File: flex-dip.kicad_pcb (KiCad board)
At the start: 2 copper layers, 19.9 x 12.9 mm, 17 parts, among them J1 Conn_01x01_Female, J10 Conn_01x01_Female, J11 Conn_01x01_Female, J12 Conn_01x01_Female, J13 Conn_01x01_Female, J14 Conn_01x01_Female, J15 Conn_01x01_Female, J16 Conn_01x01_Female, J2 Conn_01x01_Female, J3 Conn_01x01_Female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

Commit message: add gerbers
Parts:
- added REF**: OSHW-Logo2_7.3x6mm_Copper, Symbol:OSHW-Logo2_7.3x6mm_Copper, B.Cu at (119.0, 67.9)
- added REF**: OSHW-Logo2_7.3x6mm_Copper, Symbol:OSHW-Logo2_7.3x6mm_Copper, F.Cu at (119.0, 67.9)
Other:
- board text added: "2020-03-03"
- board text added: "@HelenLeigh"
- board text removed: "2020-02-06"

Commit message: update silkscreen
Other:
- board text added: "Stitch and Glitch"
- board text removed: "Crackle Flex Sew Box"
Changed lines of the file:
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@@
       (effects (font (size 1 1) (thickness 0.15)))
     )
-    (fp_line (start -1.05 8.89) (end 8.67 8.89) (layer "F.CrtYd") (width 0.1))
-    (fp_line (start -1.05 -1.29) (end -1.05 8.89) (layer "F.CrtYd") (width 0.1))
-    (fp_line (start 8.67 -1.29) (end 8.67 8.89) (layer "F.CrtYd") (width 0.1))
-    (fp_line (start -1.05 -1.29) (end 8.67 -1.29) (layer "F.CrtYd") (width 0.1))
-    (fp_line (start 0.4 -0.9) (end 0.4 -1.2) (layer "F.SilkS") (width 0.1))
-    (fp_line (start 0.4 -1.2) (end 0.7 -1.2) (layer "F.SilkS") (width 0.1))
-    (fp_line (start 7.2 -0.9) (end 7.2 -1.2) (layer "F.SilkS") (width 0.1))
-    (fp_line (start 7.2 -1.2) (end 6.9 -1.2) (layer "F.SilkS") (width 0.1))
-    (fp_line (start 7.2 8.5) (end 7.2 8.8) (layer "F.SilkS") (width 0.1))
-    (fp_line (start 7.2 8.8) (end 6.9 8.8) (layer "F.SilkS") (width 0.1))
-    (fp_line (start 0.4 8.5) (end 0.4 8.8) (layer "F.SilkS") (width 0.1))
-    (fp_line (start 0.4 8.8) (end 0.7 8.8) (layer "F.SilkS") (width 0.1))
-    (fp_line (start 0.55 8.64) (end 7.05 8.64) (layer "F.Fab") (width 0.1))
-    (fp_line (start 0.55 -1.04) (end 7.05 -1.04) (layer "F.Fab") (width 0.1))
-    (fp_line (start 7.05 -1.04) (end 7.05 8.64) (layer "F.Fab") (width 0.1))
-    (fp_line (start 0.55 -1.04) (end 0.55 8.64) (layer "F.Fab") (width 0.1))
     (fp_text user "REF**" (at 3.94 3.49) (layer "F.Fab") hide
       (effects (font (size 1 1) (thickness 0.1)))
     )
+    (fp_line (start 0.55 -1.04) (end 0.55 8.64) (layer "F.Fab") (width 0.1))
+    (fp_line (start 7.05 -1.04) (end 7.05 8.64) (layer "F.Fab") (width 0.1))
+    (fp_line (start 0.55 -1.04) (end 7.05 -1.04) (layer "F.Fab") (width 0.1))
+    (fp_line (start 0.55 8.64) (end 7.05 8.64) (layer "F.Fab") (width 0.1))
+    (fp_line (start 0.4 8.8) (end 0.7 8.8) (layer "F.SilkS") (width 0.1))
+    (fp_line (start 0.4 8.5) (end 0.4 8.8) (layer "F.SilkS") (width 0.1))
+    (fp_line (start 7.2 8.8) (end 6.9 8.8) (layer "F.SilkS") (width 0.1))
+    (fp_line (start 7.2 8.5) (end 7.2 8.8) (layer "F.SilkS") (width 0.1))
+    (fp_line (start 7.2 -1.2) (end 6.9 -1.2) (layer "F.SilkS") (width 0.1))
+    (fp_line (start 7.2 -0.9) (end 7.2 -1.2) (layer "F.SilkS") (width 0.1))
+    (fp_line (start 0.4 -1.2) (end 0.7 -1.2) (layer "F.SilkS") (width 0.1))
+    (fp_line (start 0.4 -0.9) (end 0.4 -1.2) (layer "F.SilkS") (width 0.1))
+    (fp_line (start -1.05 -1.29) (end 8.67 -1.29) (layer "F.CrtYd") (width 0.1))
+    (fp_line (start 8.67 -1.29) (end 8.67 8.89) (layer "F.CrtYd") (width 0.1))
+    (fp_line (start -1.05 -1.29) (end -1.05 8.89) (layer "F.CrtYd") (width 0.1))
+    (fp_line (start -1.05 8.89) (end 8.67 8.89) (layer "F.CrtYd") (width 0.1))
     (pad "8" thru_hole circle (at 7.62 0) (size 1.6 1.6) (drill 1) (layers *.Cu *.Mask)
       (net 6 "Net-(J11-Pad1)"))
@@
     )
   )
-  (gr_text "Crackle Flex Sew Box" (at 119.26824 61.61532) (layer "B.SilkS")
+  (gr_text "Stitch and Glitch" (at 119.26824 61.61532) (layer "B.SilkS")
     (effects (font (size 0.9 1.016) (thickness 0.1016)) (justify mirror))
   )
@@
     (effects (font (size 1.016 1.016) (thickness 0.1016)) (justify mirror))
   )
-  (gr_text "Crackle Flex Sew Box" (at 119.28348 61.62802) (layer "F.SilkS")
+  (gr_text "Stitch and Glitch" (at 119.28348 61.62802) (layer "F.SilkS")
     (effects (font (size 0.9 1.016) (thickness 0.1016)))
   )
@@
   (gr_line (start 126.1872 80.18272) (end 126.1872 61.4426) (layer "Eco1.User") (width 0.1))
   (gr_line (start 111.83366 80.25638) (end 111.83366 61.51626) (layer "Eco1.User") (width 0.1))
+  (segment (start 126.20752 71.15556) (end 128.8669 71.16318) (width 0.25) (layer "F.Cu") (net 3))
+  (segment (start 122.776161 71.141741) (end 126.20752 71.15556) (width 0.25) (layer "F.Cu") (net 3))
+  (segment (start 126.15926 68.60794) (end 128.85928 68.6054) (width 0.25) (layer "F.Cu") (net 2))
+  (segment (start 122.776161 68.601741) (end 126.15926 68.60794) (width 0.25) (layer "F.Cu") (net 2))
+  (segment (start 126.20498 66.07048) (end 128.86944 66.07556) (width 0.25) (layer "F.Cu") (net 1))
+  (segment (start 122.776161 66.061741) (end 126.20498 66.07048) (width 0.25) (layer "F.Cu") (net 1))
+  (segment (start 126.18466 63.53302) (end 128.85674 63.53556) (width 0.25) (layer "F.Cu") (net 6))
+  (segment (start 122.776161 63.521741) (end 126.18466 63.53302) (width 0.25) (layer "F.Cu") (net 6))
+  (segment (start 111.83366 71.13524) (end 115.156161 71.141741) (width 0.25) (layer "F.Cu") (net 5))
+  (segment (start 108.96854 71.13778) (end 111.83366 71.13524) (width 0.25) (layer "F.Cu") (net 5))
+  (segment (start 111.8235 68.59778) (end 115.156161 68.601741) (width 0.25) (layer "F.Cu") (net 2))
+  (segment (start 108.97108 68.59016) (end 111.8235 68.59778) (width 0.25) (layer "F.Cu") (net 2))
+  (segment (start 108.96092 66.0654) (end 111.82858 66.0654) (width 0.25) (layer "F.Cu") (net 5))
+  (segment (start 111.82858 66.0654) (end 115.156161 66.061741) (width 0.3) (layer "F.Cu") (net 5))
+  (segment (start 111.82858 63.52286) (end 115.156161 63.521741) (width 0.3) (layer "F.Cu") (net 4))
   (segment (start 108.95584 63.52286) (end 111.82858 63.52286) (width 0.3048) (layer "F.Cu") (net 4))
-  (segment (start 111.82858 63.52286) (end 115.156161 63.521741) (width 0.3) (layer "F.Cu") (net 4))
-  (segment (start 111.82858 66.0654) (end 115.156161 66.061741) (width 0.3) (layer "F.Cu") (net 5))
-  (segment (start 108.96092 66.0654) (end 111.82858 66.0654) (width 0.25) (layer "F.Cu") (net 5))
-  (segment (start 108.97108 68.59016) (end 111.8235 68.59778) (width 0.25) (layer "F.Cu") (net 2))
-  (segment (start 111.8235 68.59778) (end 115.156161 68.601741) (width 0.25) (layer "F.Cu") (net 2))
-  (segment (start 108.96854 71.13778) (end 111.83366 71.13524) (width 0.25) (layer "F.Cu") (net 5))
-  (segment (start 111.83366 71.13524) (end 115.156161 71.141741) (width 0.25) (layer "F.Cu") (net 5))
-  (segment (start 122.776161 63.521741) (end 126.18466 63.53302) (width 0.25) (layer "F.Cu") (net 6))
-  (segment (start 126.18466 63.53302) (end 128.85674 63.53556) (width 0.25) (layer "F.Cu") (net 6))
-  (segment (start 122.776161 66.061741) (end 126.20498 66.07048) (width 0.25) (layer "F.Cu") (net 1))
-  (segment (start 126.20498 66.07048) (end 128.86944 66.07556) (width 0.25) (layer "F.Cu") (net 1))
-  (segment (start 122.776161 68.601741) (end 126.15926 68.60794) (width 0.25) (layer "F.Cu") (net 2))
-  (segment (start 126.15926 68.60794) (end 128.85928 68.6054) (width 0.25) (layer "F.Cu") (net 2))
-  (segment (start 122.776161 71.141741) (end 126.20752 71.15556) (width 0.25) (layer "F.Cu") (net 3))
-  (segment (start 126.20752 71.15556) (end 128.8669 71.16318) (width 0.25) (layer "F.Cu") (net 3))
 )

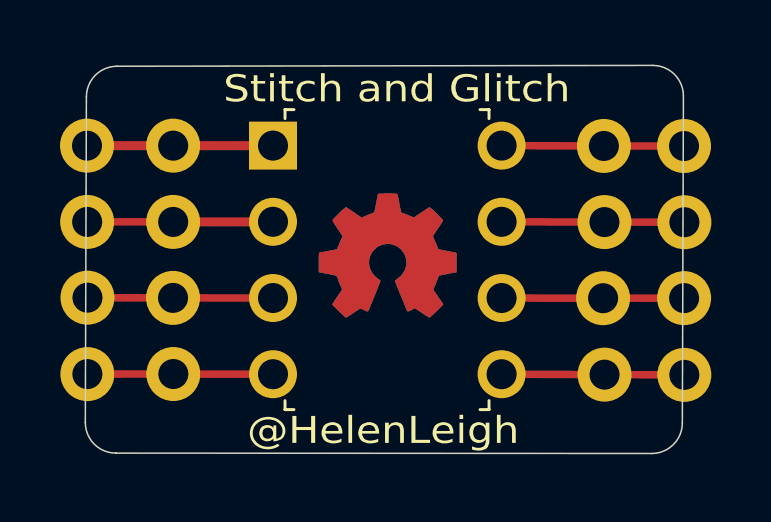
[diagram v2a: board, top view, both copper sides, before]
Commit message: put tracks on both sides with teardrops
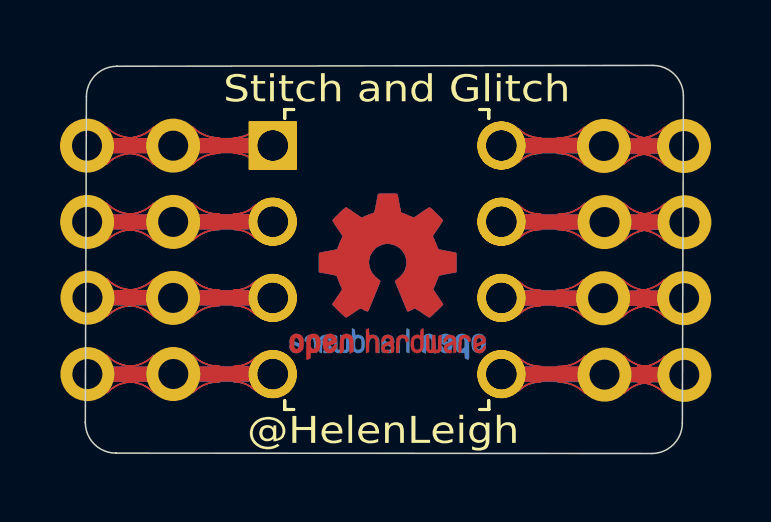
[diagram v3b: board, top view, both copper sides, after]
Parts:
- added U1: LM386, digikey-footprints:DIP-8_W7.62mm, F.Cu at (115.1, 63.5)
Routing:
- net GND: track 12.4 -> 24.8 mm
- net +3V3: track 12.3 -> 24.5 mm
- net Net-(J15-Pad1): track 6.20 -> 12.4 mm
- net Net-(J1-Pad1): track 6.09 -> 12.2 mm
- net Net-(J4-Pad1): track 6.09 -> 12.2 mm
- net Net-(J11-Pad1): track 6.08 -> 12.2 mm
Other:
- net class Default: clearance 0.2 -> 0.254; trace_width 0.25 -> 0.508
- rule trace_clearance: 0.2 -> 0.254
- board text added: "2020-03-09"
- board text removed: "2020-03-03"
